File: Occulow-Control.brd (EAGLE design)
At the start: 50.8 x 88.9 mm, 27 parts, among them J1 CORTEX_DEBUG_PTH, T1 DMP3010LK3, T2 DMP3010LK3, T3 DMP3010LK3

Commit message: routed unused header
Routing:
- net PA00: track 0.00 -> 28.5 mm
- net PA01: track 0.00 -> 26.7 mm
- net PA02: track 0.00 -> 25.8 mm
- net PA03: track 0.00 -> 25.1 mm
- net PA04: track 0.00 -> 24.4 mm
- net PA05: track 0.00 -> 23.7 mm
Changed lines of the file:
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@@
 <setting verticaltext="up"/>
 </settings>
-<grid distance="0.05" unitdist="inch" unit="inch" style="lines" multiple="1" display="no" altdistance="0.0125" altunitdist="inch" altunit="inch"/>
+<grid distance="0.05" unitdist="inch" unit="inch" style="lines" multiple="1" display="no" altdistance="0.005" altunitdist="inch" altunit="inch"/>
 <layers>
 <layer number="1" name="Top" color="4" fill="1" visible="yes" active="yes"/>
@@
 <contactref element="SL1" pad="6"/>
 <wire x1="36.5125" y1="27.2025" x2="45.46" y2="44.73" width="0" layer="19" extent="1-1"/>
-<wire x1="47.365" y1="14.885" x2="36.5125" y2="27.2025" width="0" layer="19" extent="1-1"/>
 <wire x1="30.74" y1="18.77" x2="36.5125" y2="27.2025" width="0" layer="19" extent="1-1"/>
 <wire x1="22.2525" y1="28.01" x2="30.74" y2="18.77" width="0" layer="19" extent="1-1"/>
@@
 <wire x1="3.81" y1="37.465" x2="13.183" y2="39.0525" width="0" layer="19" extent="1-1"/>
 <wire x1="4.445" y1="50.4825" x2="3.81" y2="37.465" width="0" layer="19" extent="1-1"/>
+<wire x1="47.365" y1="14.885" x2="36.5125" y2="27.2025" width="0" layer="19" extent="1-1"/>
 </signal>
 <signal name="RF">
@@
 <contactref element="U$1" pad="14"/>
 <contactref element="T2" pad="1"/>
-<wire x1="30.4525" y1="30.41" x2="42.805" y2="14.885" width="0" layer="19" extent="1-1"/>
+<wire x1="42.805" y1="14.885" x2="30.4525" y2="30.41" width="0" layer="19" extent="1-1"/>
 </signal>
 <signal name="GR_VCC">
@@
 <contactref element="U$1" pad="1"/>
 <contactref element="SL2" pad="6"/>
-<wire x1="9.2075" y1="3.81" x2="23.5525" y2="25.11" width="0" layer="19" extent="1-1"/>
+<wire x1="23.5525" y1="25.11" x2="23.5525" y2="24.1875" width="0.254" layer="1"/>
+<wire x1="23.5525" y1="24.1875" x2="20.955" y2="21.59" width="0.254" layer="1"/>
+<wire x1="20.955" y1="21.59" x2="20.955" y2="13.462" width="0.254" layer="1"/>
+<wire x1="20.955" y1="13.462" x2="15.875" y2="8.382" width="0.254" layer="1"/>
+<wire x1="15.875" y1="8.382" x2="13.7795" y2="8.382" width="0.254" layer="1"/>
+<wire x1="13.7795" y1="8.382" x2="9.2075" y2="3.81" width="0.254" layer="1"/>
 </signal>
 <signal name="PA01">
 <contactref element="U$1" pad="2"/>
 <contactref element="SL2" pad="5"/>
-<wire x1="11.7475" y1="3.81" x2="24.3525" y2="25.11" width="0" layer="19" extent="1-1"/>
+<wire x1="24.3525" y1="25.11" x2="24.3525" y2="24.0985" width="0.254" layer="1"/>
+<wire x1="24.3525" y1="24.0985" x2="21.59" y2="21.336" width="0.254" layer="1"/>
+<wire x1="21.59" y1="13.335" x2="21.59" y2="21.336" width="0.254" layer="1"/>
+<wire x1="11.7475" y1="3.81" x2="12.065" y2="3.81" width="0.254" layer="1"/>
+<wire x1="12.065" y1="3.81" x2="21.59" y2="13.335" width="0.254" layer="1"/>
 </signal>
 <signal name="PA02">
 <contactref element="U$1" pad="3"/>
 <contactref element="SL2" pad="4"/>
-<wire x1="14.2875" y1="3.81" x2="25.1525" y2="25.11" width="0" layer="19" extent="1-1"/>
+<wire x1="25.1525" y1="25.11" x2="25.1525" y2="24.1365" width="0.254" layer="1"/>
+<wire x1="25.1525" y1="24.1365" x2="22.225" y2="21.209" width="0.254" layer="1"/>
+<wire x1="22.225" y1="12.954" x2="22.225" y2="21.209" width="0.254" layer="1"/>
+<wire x1="14.2875" y1="3.81" x2="14.2875" y2="5.0165" width="0.254" layer="1"/>
+<wire x1="14.2875" y1="5.0165" x2="22.225" y2="12.954" width="0.254" layer="1"/>
 </signal>
 <signal name="PA03">
 <contactref element="U$1" pad="4"/>
 <contactref element="SL2" pad="3"/>
-<wire x1="16.8275" y1="3.81" x2="25.9525" y2="25.11" width="0" layer="19" extent="1-1"/>
+<wire x1="25.9525" y1="25.11" x2="25.9525" y2="24.1745" width="0.254" layer="1"/>
+<wire x1="25.9525" y1="24.1745" x2="22.733" y2="20.955" width="0.254" layer="1"/>
+<wire x1="22.733" y1="20.955" x2="22.733" y2="12.573" width="0.254" layer="1"/>
+<wire x1="22.733" y1="12.573" x2="16.891" y2="6.731" width="0.254" layer="1"/>
+<wire x1="16.891" y1="6.731" x2="16.891" y2="3.8735" width="0.254" layer="1"/>
+<wire x1="16.891" y1="3.8735" x2="16.8275" y2="3.81" width="0.254" layer="1"/>
 </signal>
 <signal name="PA04">
 <contactref element="U$1" pad="5"/>
 <contactref element="SL2" pad="2"/>
-<wire x1="19.3675" y1="3.81" x2="26.7525" y2="25.11" width="0" layer="19" extent="1-1"/>
+<wire x1="19.304" y1="8.001" x2="19.304" y2="3.8735" width="0.254" layer="1"/>
+<wire x1="19.304" y1="3.8735" x2="19.3675" y2="3.81" width="0.254" layer="1"/>
+<wire x1="26.7525" y1="24.0855" x2="23.368" y2="20.701" width="0.254" layer="1"/>
+<wire x1="23.368" y1="20.701" x2="23.368" y2="12.065" width="0.254" layer="1"/>
+<wire x1="26.7525" y1="25.11" x2="26.7525" y2="24.0855" width="0.254" layer="1"/>
+<wire x1="23.368" y1="12.065" x2="19.304" y2="8.001" width="0.254" layer="1"/>
 </signal>
 <signal name="PA05">
 <contactref element="U$1" pad="6"/>
 <contactref element="SL2" pad="1"/>
-<wire x1="21.9075" y1="3.81" x2="27.5525" y2="25.11" width="0" layer="19" extent="1-1"/>
+<wire x1="21.844" y1="3.8735" x2="21.844" y2="9.652" width="0.254" layer="1"/>
+<wire x1="21.844" y1="3.8735" x2="21.9075" y2="3.81" width="0.254" layer="1"/>
+<wire x1="21.844" y1="9.652" x2="23.876" y2="11.684" width="0.254" layer="1"/>
+<wire x1="23.876" y1="11.684" x2="23.876" y2="20.447" width="0.254" layer="1"/>
+<wire x1="23.876" y1="20.447" x2="27.559" y2="24.13" width="0.254" layer="1"/>
+<wire x1="27.559" y1="24.13" x2="27.559" y2="25.1035" width="0.254" layer="1"/>
+<wire x1="27.559" y1="25.1035" x2="27.5525" y2="25.11" width="0.254" layer="1"/>
 </signal>
 <signal name="PA22">

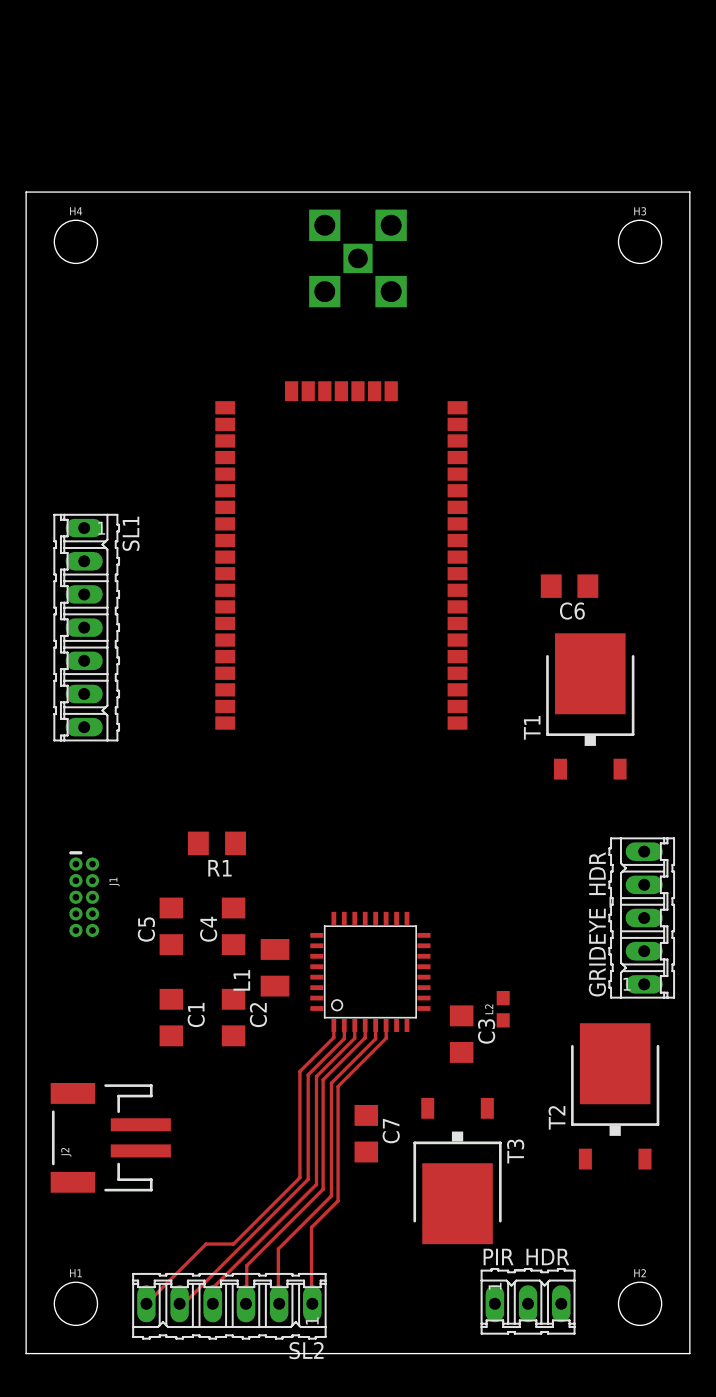
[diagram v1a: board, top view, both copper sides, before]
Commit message: Grideye, PIR, most power routing
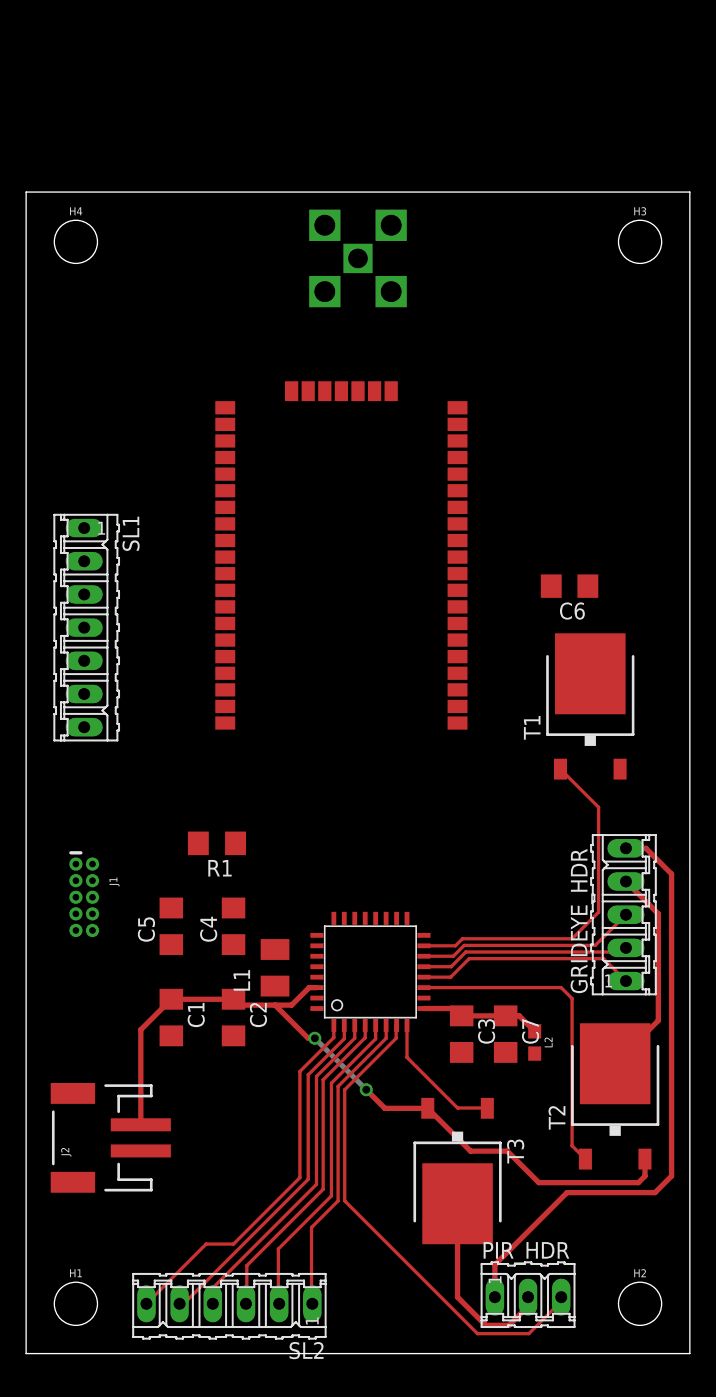
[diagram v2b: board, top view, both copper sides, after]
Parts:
- moved C7 13.1 mm to (36.7, 24.4)
- moved L2 3.50 mm to (38.9, 23.8), turned to 270 degrees
- moved GRIDEYE_HDR 1.42 mm to (45.9, 33.6)
- moved PIR_HDR 0.51 mm to (38.4, 4.32)
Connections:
- net GR_INT: now also U$1.14; no longer U$1.13
- net GR_SCL: now also U$1.13; no longer U$1.12
- net GR_SDA: now also U$1.12; no longer U$1.11
- net GR_VCC_CTL: now also U$1.11; no longer U$1.14
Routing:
- net VCC: track 0.00 -> 57.9 mm, vias 0 -> 2
- net GND: track 0.00 -> 46.2 mm
- net PIR_TRIG: track 0.00 -> 37.2 mm
- net LR_VCC_CTL: track 0.00 -> 26.6 mm
- net GR_VCC_CTL: track 0.00 -> 24.4 mm
- net GR_VCC: track 0.00 -> 17.9 mm
- net GR_INT: track 0.00 -> 16.8 mm
- net GR_SDA: track 0.00 -> 16.8 mm
- net GR_SCL: track 0.00 -> 16.1 mm
- net PIR_VCC: track 0.00 -> 14.7 mm
- net PIR_VCC_CTL: track 0.00 -> 10.2 mm
- net VDDANA: track 0.00 -> 9.20 mm

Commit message: First pass at full routing
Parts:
- moved H3 2.54 mm to (47.0, 82.5)
- moved H4 2.54 mm to (3.81, 82.5)
- moved C6 2.54 mm to (41.6, 56.2)
- moved SL1 2.54 mm to (4.45, 53.0)
- moved T1 2.54 mm to (43.2, 47.0)
- moved U$2 2.54 mm to (24.1, 57.1)
- moved U$3 2.54 mm to (25.4, 81.3)
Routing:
- net GND: track 46.2 -> 362.2 mm
- net VCC: track 57.9 -> 149.3 mm, vias 2 -> 3
- net LR_RST_N: track 0.00 -> 50.3 mm, vias 0 -> 2
- net PA22: track 0.00 -> 40.6 mm
- net PA23: track 0.00 -> 37.6 mm
- net LR_VCC: track 0.00 -> 37.0 mm
- net PA24: track 0.00 -> 34.9 mm
- net PA25: track 0.00 -> 32.2 mm
- net SWCLK: track 0.00 -> 29.8 mm, vias 0 -> 2
- net PA27: track 0.00 -> 27.8 mm, vias 0 -> 1
- net LR_RX: track 0.00 -> 23.1 mm
- net SWDIO: track 0.00 -> 22.1 mm, vias 0 -> 1
- net LR_TX: track 0.00 -> 21.4 mm
- net !RESET: track 0.00 -> 20.2 mm
- net LR_CTS: track 0.00 -> 17.3 mm
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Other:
- board size 50.8 x 88.9 mm -> 50.8 x 86.4 mm

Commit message: Moved center
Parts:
- moved FRAME1 56.2 mm to (25.4, 44.5)
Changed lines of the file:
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@@
 <element name="C6" library="rcl" package="C1206" value="10uF" x="41.5925" y="56.1975" rot="R180"/>
 <element name="C7" library="rcl" package="C1206" value="10uF" x="36.703" y="24.4475" rot="R270"/>
-<element name="FRAME1" library="SparkFun-Aesthetics" package="DUMMY" value="FRAME-LETTERNO_PACKAGE" x="-25.4" y="68.58">
-<attribute name="DESIGNER" value="Nobody" x="-25.4" y="68.58" size="1.778" layer="27" display="off"/>
-<attribute name="VERSION" value="v01" x="-25.4" y="68.58" size="1.778" layer="27" display="off"/>
+<element name="FRAME1" library="SparkFun-Aesthetics" package="DUMMY" value="FRAME-LETTERNO_PACKAGE" x="25.4" y="44.45">
+<attribute name="DESIGNER" value="Nobody" x="25.4" y="44.45" size="1.778" layer="27" display="off"/>
+<attribute name="VERSION" value="v01" x="25.4" y="44.45" size="1.778" layer="27" display="off"/>
 </element>
 <element name="GRIDEYE_HDR" library="con-amp-quick" package="05P" value="" x="45.9105" y="33.5915" rot="R90">

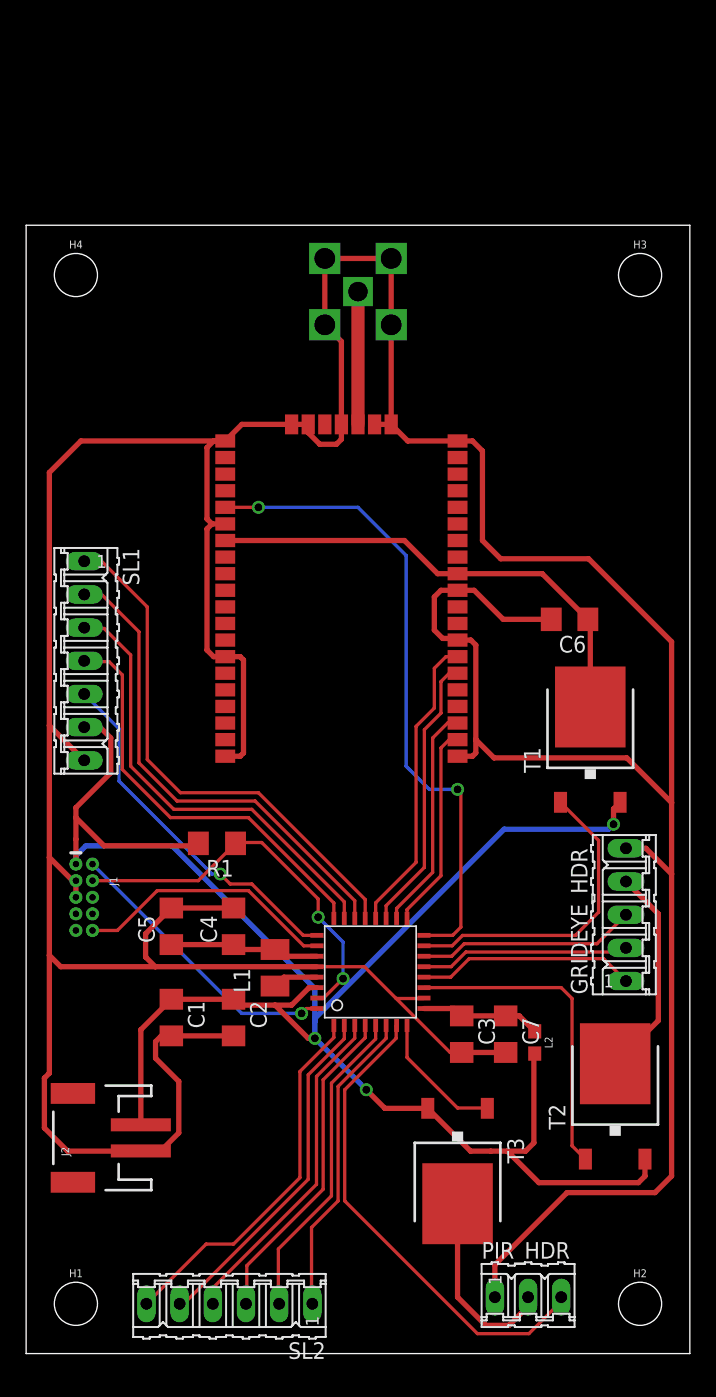
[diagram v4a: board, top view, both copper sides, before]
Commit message: Added vias for RF
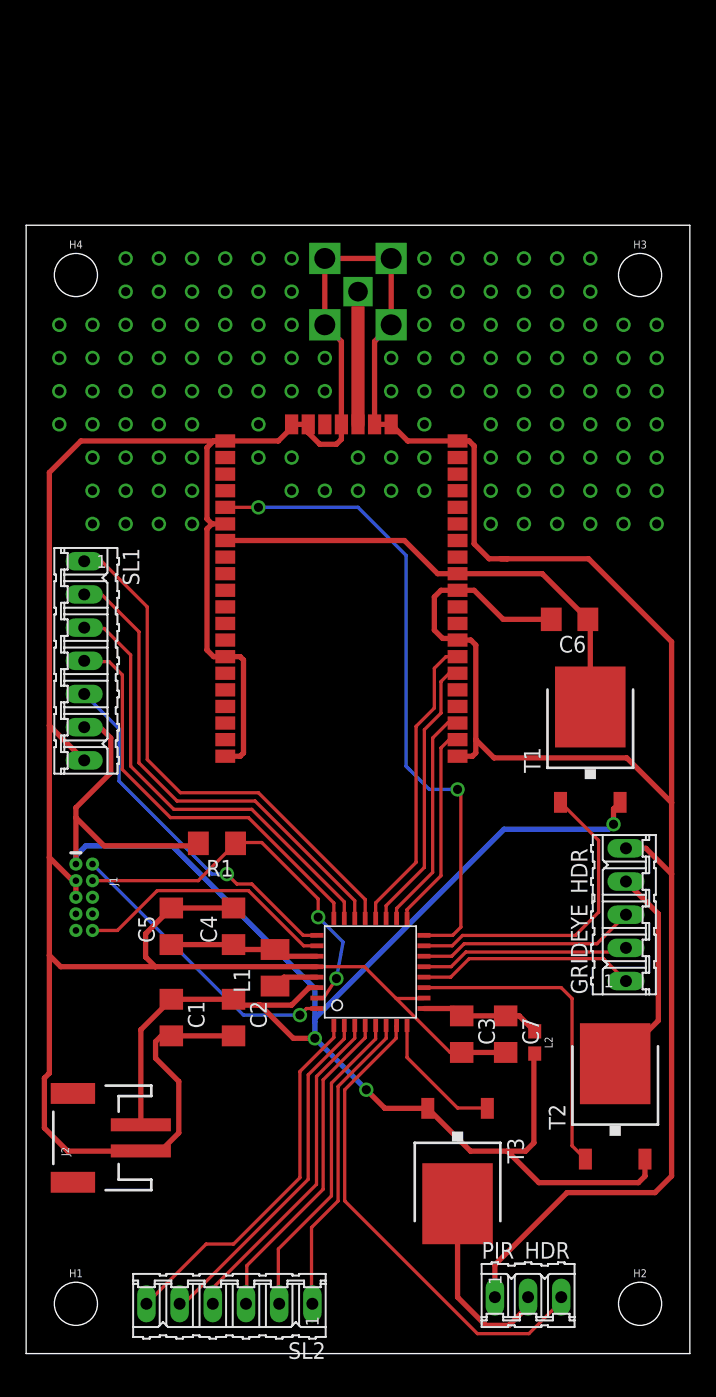
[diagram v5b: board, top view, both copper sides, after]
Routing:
- net GND: track 362.2 -> 363.8 mm
- net VCC: track 149.3 -> 150.3 mm

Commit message: SAM portion fully routed
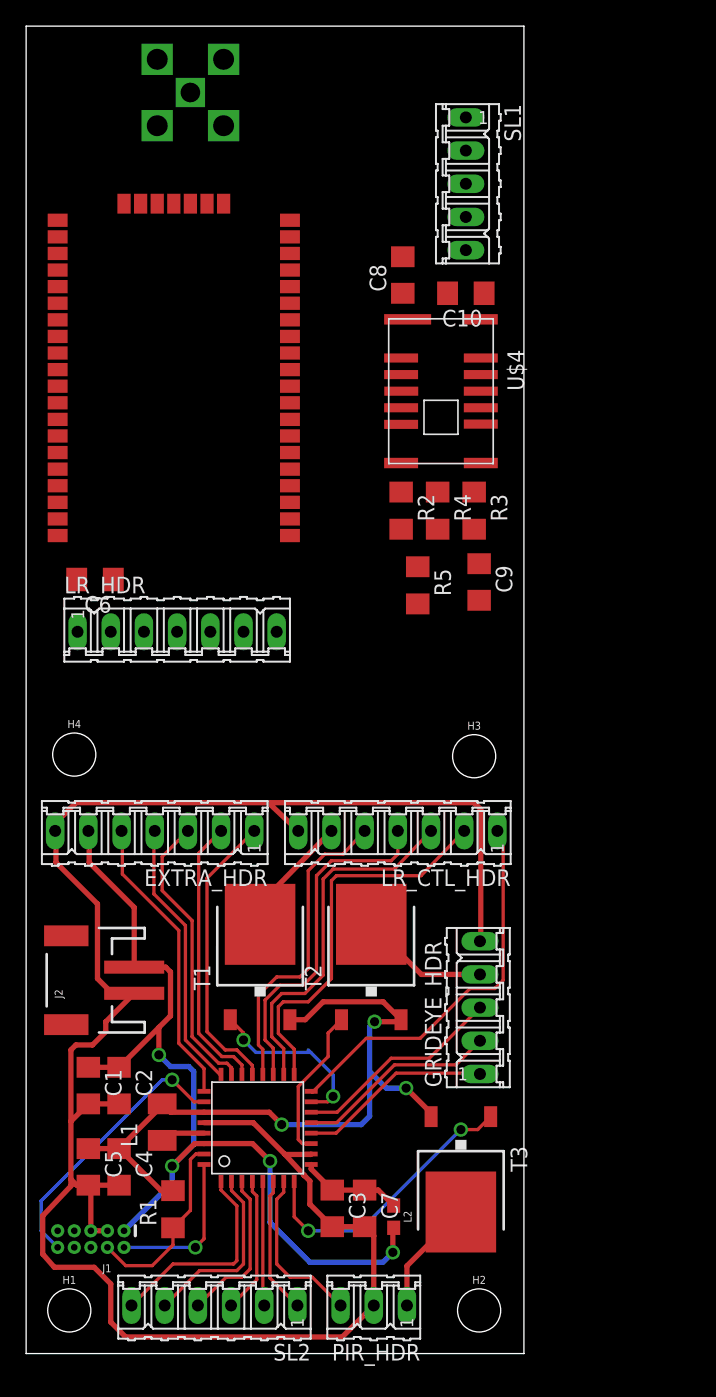
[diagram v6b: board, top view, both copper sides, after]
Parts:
- added C10: 1.5 uF, rcl:C1206
- added C8: 10 uF, rcl:C1206
- added C9: 1 uF, rcl:C1206
- added EXTRA_HDR, LR_CTL_HDR, LR_HDR: (no value), con-amp-quick:07P
- added FRAME2, FRAME3: FRAME-LETTERNO_PACKAGE, SparkFun-Aesthetics:DUMMY
- added R2, R3, R4: 10k, resistor:R1206
- added R5: 20, resistor:R1206
- added U$4: AMG8833SMD, GridEye:AMG8833
- SL1: device con-amp-quick:07P -> con-amp-quick:05P
- moved SL1 46.8 mm to (33.7, 89.5)
- moved H3 39.0 mm to (34.3, 45.7)
- moved H4 36.7 mm to (3.68, 45.8)
- moved C6 36.4 mm to (5.27, 59.2)
- moved T1 30.3 mm to (17.9, 30.4)
- moved R1 28.2 mm to (11.2, 11.0), turned to 90 degrees
- moved J1 26.2 mm to (4.95, 8.76), turned to 180 degrees
- moved T2 21.5 mm to (26.4, 30.4)
- moved U$2 21.2 mm to (11.3, 74.0)
- moved C4 20.4 mm to (7.11, 14.3), turned to 270 degrees
- moved U$3 19.9 mm to (12.6, 96.5)
- moved C5 19.5 mm to (4.76, 14.3), turned to 270 degrees
- moved C7 17.2 mm to (25.9, 11.1)
- moved L2 17.2 mm to (28.1, 10.5)
- moved C3 16.6 mm to (23.4, 11.1)
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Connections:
- new net GR_GND: C10.2, C8.2, R5.1, SL1.5, U$4.5, U$4.6
- new net GR_INT_HDR: GRIDEYE_HDR.3, U$1.14
- new net GR_SCL_HDR: GRIDEYE_HDR.2, U$1.13
- new net GR_SDA_HDR: GRIDEYE_HDR.1, U$1.12
- new net GR_VCC_HDR: GRIDEYE_HDR.4, T2.3
- new net LR_CTS_HDR: LR_CTL_HDR.3, U$1.18
- new net LR_GND: C6.2, LR_HDR.1, U$2.1, U$2.11, U$2.20, U$2.21, U$2.22, U$2.24, U$2.26, U$2.27, U$2.28, U$2.33, U$2.41, U$2.47, U$2.8, U$3.1, U$3.2, U$3.3, U$3.4
- new net LR_RST_N_HDR: LR_CTL_HDR.1, U$1.16
- new net LR_RTS_HDR: LR_CTL_HDR.2, U$1.17
- new net LR_RX_HDR: LR_CTL_HDR.5, U$1.20
- new net LR_TX_HDR: LR_CTL_HDR.4, U$1.19
- new net LR_VCC_HDR: LR_CTL_HDR.6, T1.3
- new net N$2: C9.1, U$4.10
- new net N$3: C9.2, R5.2
- new net N$4: C10.1, U$4.12
- net GND: now also EXTRA_HDR.7, LR_CTL_HDR.7, PIR_HDR.2; no longer C6.2, PIR_HDR.1, SL1.7, U$2.1, U$2.11, U$2.20, U$2.21, U$2.22, U$2.24, U$2.26, U$2.27, U$2.28, U$2.33, U$2.41, U$2.47, U$2.8, U$3.1, U$3.2, U$3.3, U$3.4
- net GR_INT: now also R2.1, SL1.1, U$4.4; no longer GRIDEYE_HDR.3, U$1.14
- net GR_SCL: now also R4.1, SL1.2, U$4.3; no longer GRIDEYE_HDR.2, U$1.13
- net GR_SDA: now also R3.1, SL1.3, U$4.2; no longer GRIDEYE_HDR.1, U$1.12
- net GR_VCC: now also C8.1, R2.2, R3.2, R4.2, SL1.4, U$4.13, U$4.9; no longer GRIDEYE_HDR.4, T2.3
- net LR_CTS: now also LR_HDR.6; no longer U$1.18
- net LR_RST_N: now also LR_HDR.3; no longer U$1.16
- net LR_RTS: now also LR_HDR.7; no longer U$1.17
- net LR_RX: now also LR_HDR.4; no longer U$1.20
- net LR_TX: now also LR_HDR.5; no longer U$1.19
- net LR_VCC: now also LR_HDR.2; no longer T1.3
- net PA22: now also EXTRA_HDR.1; no longer SL1.1
- net PA23: now also EXTRA_HDR.2; no longer SL1.2
- net PA24: now also EXTRA_HDR.3; no longer SL1.3
- net PA25: now also EXTRA_HDR.4; no longer SL1.4
- net PA27: now also EXTRA_HDR.5; no longer SL1.5
- net PIR_VCC: now also PIR_HDR.1; no longer PIR_HDR.2
- net VCC: now also EXTRA_HDR.6; no longer R1.2, SL1.6, T1.2, T2.2, T3.2
- net VDDCORE: now also R1.2, T1.2, T2.2, T3.2
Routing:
- net GND: track 363.8 -> 155.5 mm
- net VCC: track 150.3 -> 72.1 mm, vias 3 -> 4
- net LR_RST_N: track 50.3 -> 0.00 mm, vias 2 -> 0
- net VDDCORE: track 11.5 -> 54.8 mm, vias 0 -> 3
- net LR_VCC: track 37.0 -> 0.00 mm
- net LR_RST_N_HDR: track 0.00 -> 30.9 mm
- net LR_RTS_HDR: track 0.00 -> 29.9 mm
- net LR_CTS_HDR: track 0.00 -> 27.8 mm
- net LR_TX_HDR: track 0.00 -> 26.8 mm
- net PIR_TRIG: track 37.2 -> 12.7 mm
- net LR_RX_HDR: track 0.00 -> 24.0 mm
- net LR_RX: track 23.1 -> 0.00 mm
- net LR_TX: track 21.4 -> 0.00 mm
- net PA22: track 40.6 -> 22.1 mm
- net GR_VCC: track 17.9 -> 0.00 mm
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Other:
- board size 50.8 x 86.4 mm -> 38.1 x 101.6 mm
